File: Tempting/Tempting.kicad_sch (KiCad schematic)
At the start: 50 parts, among them J1 Conn_Coaxial, J2 Conn_01x07_Socket, J3 Conn_ARM_SWD_TagConnect_TC2030, J4 USB_C_Receptacle_USB2.0_16P, SW1 SPST, SW2 SPST, U1 AMS1117-3.3, U2 SCD41-D-R2, U3 STM32WB55CGUx, U4 DPS368, U5 USBLC6-2SC6, X1 32M, X2 32.768k

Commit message: Rough initial layout
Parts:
- added C10, C12: 4.7u, Capacitor_SMD:C_0603_1608Metric, symbol Device:C
- added C15: 100n, Capacitor_SMD:C_0402_1005Metric, symbol Device:C
- renumbered C10 to C11, C11 to C13, C12 to C14, C14 to C16, C15 to C17, C13 to C18, C16 to C19, C17 to C20, C18 to C21, C19 to C22, C20 to C23, C21 to C24, C22 to C25
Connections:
- net +3.3V: now also C10.1, C12.1, C15.1
- net BUTTON_1: now also SW1.3 (K)
- net BUTTON_2: now also SW2.3 (K)
- net GND: now also SW1.2, SW2.2, C10.2, C12.2, C15.2
- net LED_R: now reaches D1.1 (RK), R2.2
- net LED_G: now reaches D1.3 (GK), R3.2
- net LED_B: now reaches D1.4 (BK), R4.2
- net LED_R_MCU: now reaches R2.1, U3.9 (PA0)
- net LED_G_MCU: now reaches R3.1, U3.10 (PA1)
- net LED_B_MCU: now reaches R4.1, U3.11 (PA2)
- net MCU_SMPSFB renamed SMPSFB_MCU
- net MCU_SMPSLX renamed SMPSLX_MCU
- no-connect marks 18 -> 14
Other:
- moved on the sheet: C18, U2

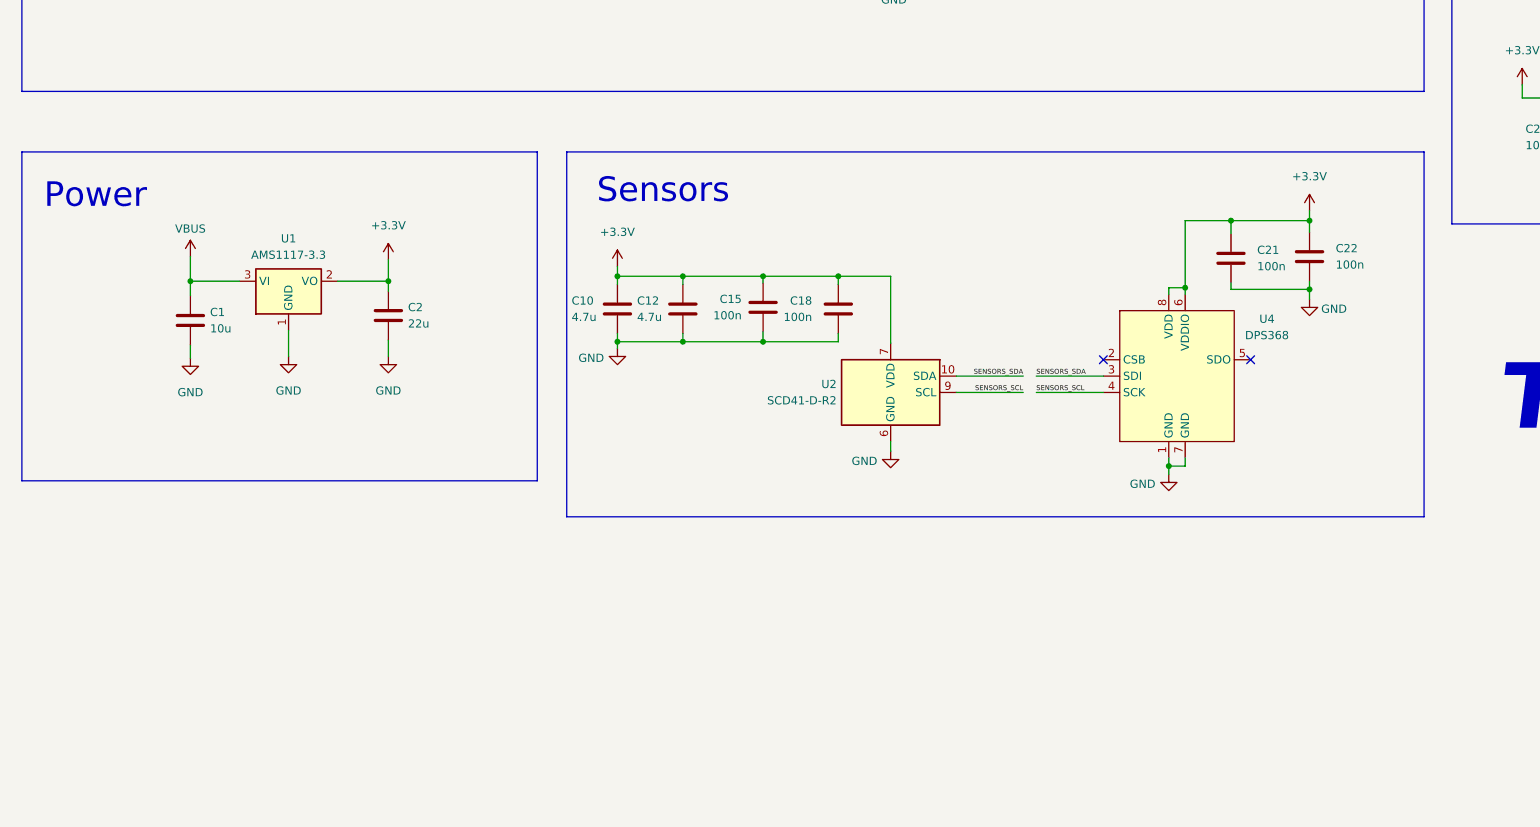
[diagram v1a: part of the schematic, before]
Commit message: Added edge cuts and mounting holes
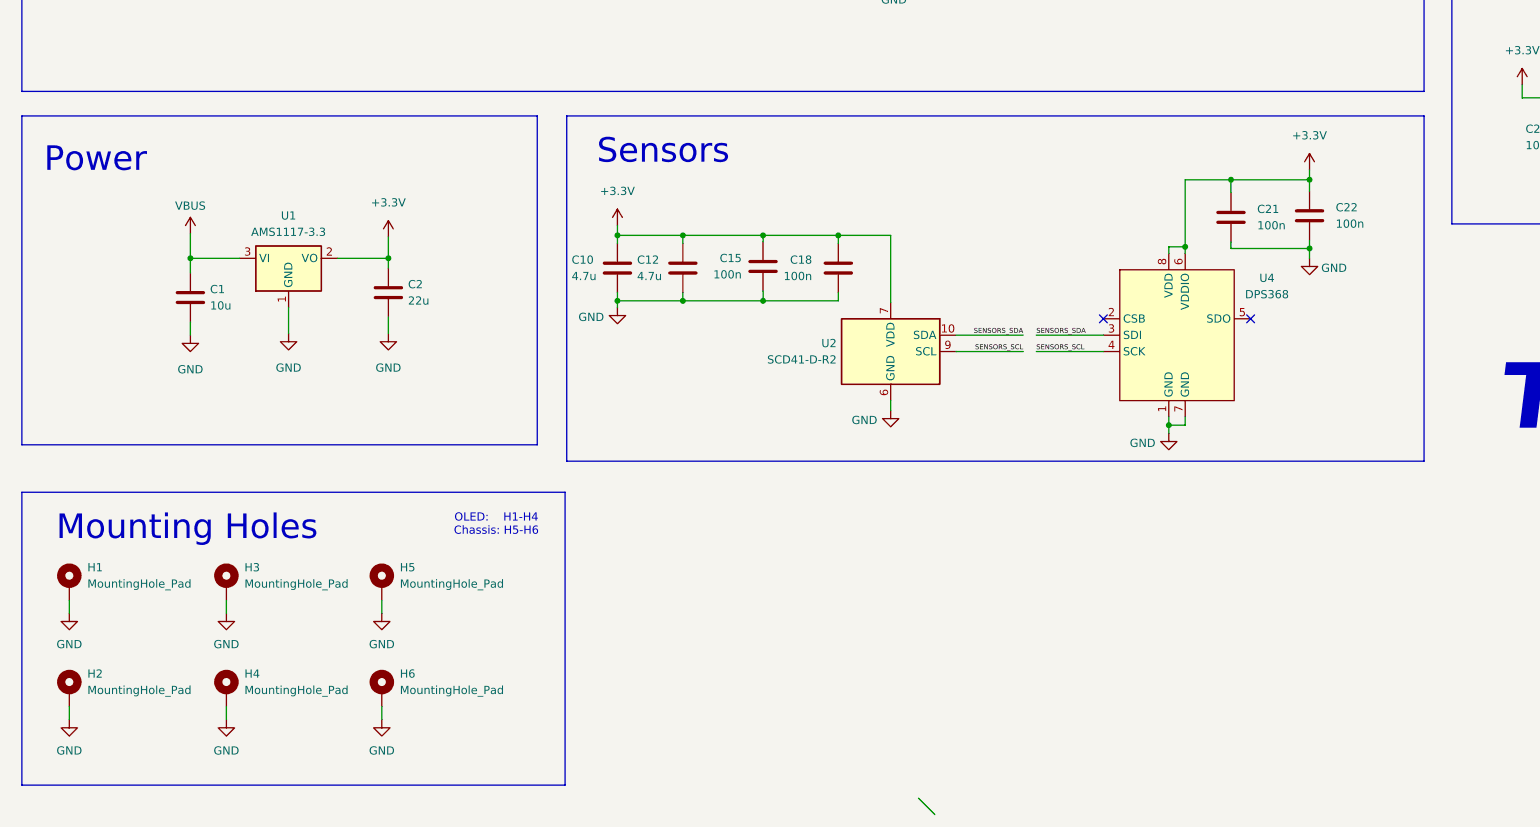
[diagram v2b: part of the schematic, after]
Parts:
- added H1, H2, H3, H4: MountingHole_Pad, MountingHole:MountingHole_2.2mm_M2_Pad_Via, symbol Mechanical:MountingHole_Pad
- added H5, H6: MountingHole_Pad, MountingHole:MountingHole_3.2mm_M3_Pad_Via, symbol Mechanical:MountingHole_Pad
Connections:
- net GND: now also H1.1, H2.1, H3.1, H4.1, H5.1, H6.1
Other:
- note added: "Mounting Holes"
- note added: "OLED: H1-H4 Chassis: H5-H6"
- moved on the sheet: C1, C10, C12, C15, C18, C2, C21, C22, U1, U2, U4

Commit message: Finetuned layout
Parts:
- added C3, C7: 100n, Capacitor_SMD:C_0402_1005Metric, symbol Device:C
- renumbered C8 to C10, C9 to C11, C10 to C12, C11 to C13, C12 to C14, C13 to C15, C14 to C16, C15 to C17, C16 to C18, C17 to C19, C5 to C2, C18 to C20, C19 to C21, C20 to C22, C21 to C23, C22 to C24, C23 to C25, C24 to C26, C25 to C27, C2 to C4, C3 to C5, C4 to C6, C6 to C8, C7 to C9
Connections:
- net +3.3V: now also C3.1, C7.1
- net GND: now also C3.2, C7.2
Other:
- moved on the sheet: C2

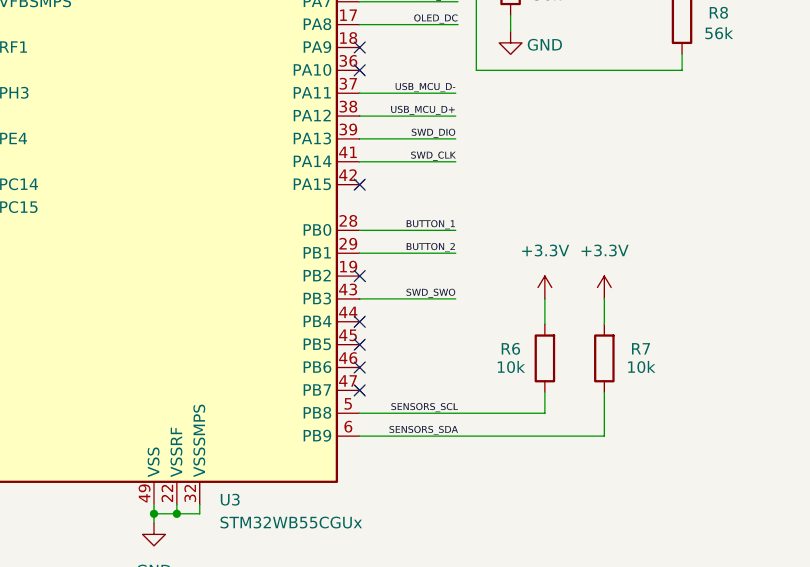
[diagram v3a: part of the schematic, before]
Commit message: All signal traces routed
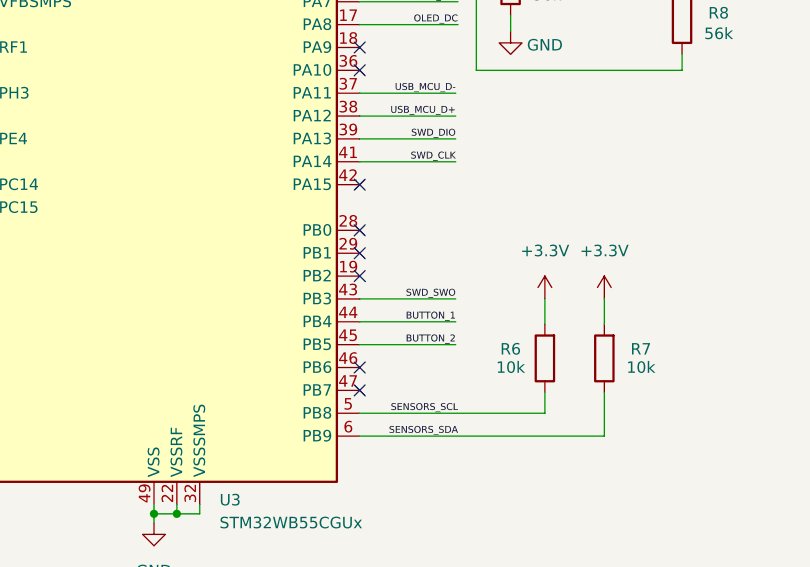
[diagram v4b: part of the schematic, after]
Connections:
- net BUTTON_1: now also U3.44 (PB4); no longer U3.28 (PB0)
- net BUTTON_2: now also U3.45 (PB5); no longer U3.29 (PB1)
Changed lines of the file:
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@@
 	)
 	(no_connect
-		(at 178.816 127.254)
+		(at 178.816 117.094)
 	)
 	(no_connect
@@
 	)
 	(no_connect
-		(at 178.816 129.794)
+		(at 178.816 119.634)
 	)
 	(no_connect
@@
 	(wire
 		(pts
-			(xy 178.816 119.634) (xy 189.484 119.634)
-		)
-		(stroke
-			(width 0)
-			(type default)
-		)
-	)
-	(wire
-		(pts
 			(xy 299.212 43.18) (xy 299.212 44.704)
 		)
@@
 	(wire
 		(pts
+			(xy 178.816 129.794) (xy 189.484 129.794)
+		)
+		(stroke
+			(width 0)
+			(type default)
+		)
+	)
+	(wire
+		(pts
 			(xy 79.248 130.048) (xy 83.312 130.048)
 		)
@@
 	(wire
 		(pts
+			(xy 178.816 127.254) (xy 189.484 127.254)
+		)
+		(stroke
+			(width 0)
+			(type default)
+		)
+	)
+	(wire
+		(pts
 			(xy 214.63 97.536) (xy 214.63 99.314)
 		)
@@
 	(wire
 		(pts
-			(xy 178.816 117.094) (xy 189.484 117.094)
-		)
-		(stroke
-			(width 0)
-			(type default)
-		)
-	)
-	(wire
-		(pts
 			(xy 220.472 182.88) (xy 208.28 182.88)
 		)
@@
 	)
 	(label "BUTTON_1"
+		(at 189.484 127.254 180)
+		(fields_autoplaced yes)
+		(effects
+			(font
+				(size 0.762 0.762)
+			)
+			(justify right bottom)
+		)
+	)
+	(label "BUTTON_1"
 		(at 320.802 154.94 180)
 		(fields_autoplaced yes)
@@
 		)
 	)
-	(label "SENSORS_SCL"
-		(at 189.738 137.414 180)
+	(label "BUTTON_2"
+		(at 189.484 129.794 180)
 		(fields_autoplaced yes)
 		(effects
@@
 		)
 	)
-	(label "BUTTON_1"
-		(at 189.484 117.094 180)
+	(label "SENSORS_SCL"
+		(at 189.738 137.414 180)
 		(fields_autoplaced yes)
 		(effects
@@
 		)
 	)
-	(label "BUTTON_2"
-		(at 189.484 119.634 180)
-		(fields_autoplaced yes)
-		(effects
-			(font
-				(size 0.762 0.762)
-			)
-			(justify right bottom)
-		)
-	)

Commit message: Assigned JLCPCB part numbers to all components
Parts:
- C1, C25: JLCPCB Part # (none) -> C15850
- C10, C13, C16, C17, C18, C19, C20, C21, C23, C24, C26, C27, C3, C6, C7: JLCPCB Part # (none) -> C1525
- C11, C15: value C -> 10p; JLCPCB Part # (none) -> C161145
- C12, C14, C2, C22, C9: JLCPCB Part # (none) -> C1705
- C4: JLCPCB Part # (none) -> C29277
- C5: JLCPCB Part # (none) -> C880415
- C8: JLCPCB Part # (none) -> C76915
- D1: JLCPCB Part # (none) -> C5547384
- FLT1: JLCPCB Part # (none) -> C531364
- J1: JLCPCB Part # (none) -> C434812
- J4: JLCPCB Part # (none) -> C165948
- L1: JLCPCB Part # (none) -> C77108
- L2: JLCPCB Part # (none) -> C98030
- L3: JLCPCB Part # (none) -> C76760
- R1, R6, R7: JLCPCB Part # (none) -> C25744
- R10, R9: JLCPCB Part # (none) -> C25905
- R2: JLCPCB Part # (none) -> C25132
- R3, R4: JLCPCB Part # (none) -> C4125
- R5, R8: JLCPCB Part # (none) -> C25796
- SW1, SW2: JLCPCB Part # (none) -> C513492
- U1: JLCPCB Part # (none) -> C6186
- U2: JLCPCB Part # (none) -> C3659362
- U3: JLCPCB Part # (none) -> C404023
- U4: JLCPCB Part # (none) -> C3232508
- U5: JLCPCB Part # (none) -> C7519
- X1: JLCPCB Part # (none) -> C1986260
- X2: JLCPCB Part # (none) -> C528982

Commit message: Updated ufl connector to sma
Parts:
- J1: footprint Connector_Coaxial:U.FL_Hirose_U.FL-R-SMT-1_Vertical -> Connector_Coaxial:SMA_Samtec_SMA-J-P-H-ST-EM1_EdgeMount; JLCPCB Part # C434812 -> C5199907
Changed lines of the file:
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@@
 			)
 		)
-		(property "Footprint" "Connector_Coaxial:U.FL_Hirose_U.FL-R-SMT-1_Vertical"
+		(property "Footprint" "Connector_Coaxial:SMA_Samtec_SMA-J-P-H-ST-EM1_EdgeMount"
 			(at 39.37 96.774 0)
 			(effects
@@
 			)
 		)
-		(property "JLCPCB Part #" "C434812"
+		(property "JLCPCB Part #" "C5199907"
 			(at 39.37 96.774 0)
 			(effects
